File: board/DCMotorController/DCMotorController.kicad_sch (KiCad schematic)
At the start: 129 parts, among them J2 Conn_01x03_Female, M1+1 Conn_01x01_Female, M1-1 Conn_01x01_Female, M1_S1 Conn_01x03_Female, M1_S2 Conn_01x03_Female, M2+1 Conn_01x01_Female, M2-1 Conn_01x01_Female, M2_S1 Conn_01x03_Female, M2_S2 Conn_01x03_Female, Q1 Q_NMOS_GDS, Q10 Q_NMOS_GDS, Q11 Q_NMOS_GDS, Q12 Q_NMOS_GDS, Q13 Q_NMOS_GDS, Q14 Q_NMOS_GDS, Q15 Q_NMOS_GDS, Q16 Q_NMOS_GDS, Q2 Q_NMOS_GDS, Q3 Q_NMOS_GDS, Q4 Q_NMOS_GDS, Q5 Q_NMOS_GDS, Q6 Q_NMOS_GDS, Q7 Q_NMOS_GDS, Q8 Q_NMOS_GDS, Q9 Q_NMOS_GDS, U1 DS18B20, U10 TPS54360DDA, U2 IR2103, U3 IR2103, U4 ESP32-WROOM-32D, U5 IR2103, U6 IR2103, U7 TPS54360DDA, U8 AMS1117-3.3, U9 DS18B20

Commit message: first version + test firmeware
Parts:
- added C42, C43, C44: 1500uF, Capacitor_THT:C_Radial_D10.0mm_H12.5mm_P5.00mm, symbol Device:C_Polarized
- added D20: WS2812B, LED_SMD:LED_WS2812B_PLCC4_5.0x5.0mm_P3.2mm, symbol LED:WS2812B
- added R23, R24, R25, R26: 10k, Resistor_SMD:R_0603_1608Metric, symbol Device:R
- Boot1: LCSC storage -> C72443; LCSC_PART_NUMBER C72443 -> (none)
- C1, C2, C5: LCSC yes -> C49678; LCSC_PART_NUMBER C49678 -> (none)
- C10, C12, C15, C25, C28, C33: LCSC yes -> C14663; LCSC_PART_NUMBER C14663 -> (none)
- C11, C13, C14, C26, C27, C7, C8, C9: LCSC yes -> C13585; LCSC_PART_NUMBER C13585 -> (none)
- C16, C18, C37, C38: footprint Resistor_SMD:R_1206_3216Metric -> Capacitor_SMD:C_1206_3216Metric; LCSC fix footrpint -> C96123; LCSC_PART_NUMBER C96123 -> (none)
- C17: LCSC fix footprint -> C59461
- C19, C20, C31, C32: footprint Capacitor_SMD:C_0603_1608Metric -> Capacitor_SMD:C_1206_3216Metric; LCSC lcsc -> C920964; LCSC_PART_NUMBER C920964 -> (none)
- C21, C22, C35, C36: LCSC lcsc -> C1666
- C23: footprint Capacitor_THT:C_Radial_D18.0mm_H35.5mm_P7.50mm -> Capacitor_THT:CP_Radial_D25.0mm_P10.00mm_SnapIn; LCSC lcsc -> C316460
- C24, C34: LCSC yes -> C1631; LCSC_PART_NUMBER C1631 -> (none)
- C29, C39, C40, C41: LCSC yes -> C16780; LCSC_PART_NUMBER C16780 -> (none)
- C3, C4, C6: LCSC yes -> C5674; LCSC_PART_NUMBER C45783 -> (none)
- C30: LCSC lcsc -> C503217; LCSC_PART_NUMBER C503217 -> (none)
- D1, D11, D4, D8: LCSC yes -> C412437; LCSC_PART_NUMBER C412437 -> (none)
- D10, D12, D13, D2, D5, D6, D7, D9: LCSC yes -> C81598; LCSC_PART_NUMBER C81598 -> (none)
- D14, D15, D16, D17, D3: LCSC no -> C397601
- D18: LCSC no -> C85100; LCSC_PART_NUMBER C266541 -> (none)
- D19: LCSC yes -> C191023; LCSC_PART_NUMBER C191023 -> (none)
- L1: LCSC no -> C2761921
- L2: LCSC no -> C2847544
- Q1, Q10, Q11, Q12, Q13, Q14, Q15, Q16, Q2, Q3, Q4, Q5, Q6, Q7, Q8, Q9: LCSC (none) -> C110912; LCSC_PART_NUMBER C2838123 -> (none)
- R1, R17, R2: footprint Resistor_SMD:R_0805_2012Metric -> Resistor_SMD:R_0603_1608Metric; LCSC (none) -> C21190; LCSC_PART_NUMBER C95781 -> (none)
- R10, R3, R4, R5, R6, R7, R8, R9: value ~100ohm -> 15; LCSC (none) -> C22810
- R11: value 0ohm -> 15; footprint Resistor_SMD:R_0603_1608Metric_Pad0.98x0.95mm_HandSolder -> Resistor_SMD:R_0603_1608Metric; LCSC (none) -> C22810
- R12, R22: footprint Capacitor_SMD:C_0603_1608Metric -> Resistor_SMD:R_0603_1608Metric; LCSC (none) -> C22797
- R13: LCSC (none) -> C21190; LCSC_PART_NUMBER C95781 -> (none)
- R14, R15: LCSC (none) -> C21190; LCSC_PART_NUMBER C212284 -> (none)
- R16: LCSC (none) -> C25804; LCSC_PART_NUMBER C212284 -> (none)
- R18, R19, R20, R21: LCSC (none) -> C23254; LCSC_PART_NUMBER C23254 -> (none)
- Reset1: LCSC (none) -> C72443; LCSC_PART_NUMBER C72443 -> (none)
- Rvoltage1, Rvoltage2, Rvoltage4: footprint Capacitor_SMD:C_0603_1608Metric -> Resistor_SMD:R_0603_1608Metric
- Rvoltage3: footprint Capacitor_SMD:C_0603_1608Metric -> Resistor_SMD:R_0603_1608Metric; LCSC (none) -> C22797; LCSC_PART_NUMBER C22797 -> (none)
- U10, U7: LCSC yes -> C44377; LCSC_PART_NUMBER C44377 -> (none)
- U2, U3, U5, U6: LCSC (none) -> C111908; LCSC_PART_NUMBER C111908 -> (none)
- U4: LCSC (none) -> C529578; LCSC_PART_NUMBER C529578 -> (none)
- U8: LCSC yes -> C96123; LCSC_PART_NUMBER C6186 -> (none)
- renumbered J2 to GND_TX_RX1
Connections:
- net CUSTOM_GPIO12 is gone; now on net M1_S2: U4.14 (IO12)
- net PLANT_CTRL_PUMP_1 is gone; now on net M2_S2: U4.29 (IO5)
- net PUMP_ENABLE is gone; now on net M2_S1: U4.16 (IO13)
- net SENSORS_ENABLE is gone; now on net M1_S1: U4.13 (IO14)
- net 3_3V: now also D20.1 (VDD)
- net 5V: no longer U8.3 (VI)
- net GND: now also Boot1.1, C1.1, C42.2, C43.2, C44.2, D20.3 (VSS)
- net M1_S1: now also R23.2; no longer M1_S1.3 (Pin_3)
- net M1_S2: now also R24.2; no longer M1_S2.3 (Pin_3)
- net M2_S1: now also R25.2; no longer M2_S1.3 (Pin_3)
- net M2_S2: now also R26.2; no longer M2_S2.3 (Pin_3)
- net VIN: now also C42.1, C43.1, C44.1
- net VMosfet: now also U8.3 (VI)
- net PLANT0_MOIST: no longer names the net of U4.8 (IO32)
- net PLANT0_MOIST: now also D20.4 (DIN)
- new net: M1_S1.3 (Pin_3), R23.1
- new net: M1_S2.3 (Pin_3), R24.1
- new net: M2_S1.3 (Pin_3), R25.1
- new net: M2_S2.3 (Pin_3), R26.1
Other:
- moved on the sheet: M1_S1, M1_S2, M2_S1, M2_S2

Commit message: Allegro current sensor edition
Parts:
- removed C15: 100nF, Capacitor_SMD:C_0603_1608Metric, symbol Device:C
- removed C16, C18: 47uF, Capacitor_SMD:C_1206_3216Metric, symbol Device:C
- removed C19, C20: 2.2uF 60V, Capacitor_SMD:C_1206_3216Metric, symbol Device:C
- removed C21, C22: 39pf, Capacitor_SMD:C_0603_1608Metric, symbol Device:C
- removed C24: 6800pF, Capacitor_SMD:C_0603_1608Metric, symbol Device:C
- removed C30: 1000uF, Capacitor_THT:CP_Radial_D10.0mm_P5.00mm, symbol Device:CP
- removed C44: 1500uF, Capacitor_THT:C_Radial_D10.0mm_H12.5mm_P5.00mm, symbol Device:C_Polarized
- removed D18: B560C, Diode_SMD:D_SMC_Handsoldering, symbol Device:D
- removed L1: 8.2uH, Inductor_SMD:L_12x12mm_H8mm, symbol Device:L
- removed R12: 13k, Resistor_SMD:R_0603_1608Metric, symbol Device:R
- removed R19, R21: 82k, Resistor_SMD:R_0603_1608Metric_Pad0.98x0.95mm_HandSolder, symbol Device:R
- removed Rvoltage1: 5.24*Rvoltage2 (5,6 - 7.5), Resistor_SMD:R_0603_1608Metric, symbol Device:R
- removed Rvoltage2: 1k 1.4k, Resistor_SMD:R_0603_1608Metric, symbol Device:R
- removed U7: TPS54360DDA, Package_SO:TI_SO-PowerPAD-8_ThermalVias, symbol Regulator_Switching:TPS54360DDA
- added C? (x2): 100nF, Capacitor_SMD:C_0603_1608Metric, symbol Device:C
- added R? (x2): 1k, Resistor_SMD:R_0603_1608Metric, symbol Device:R
- added U11, U7: ACS758xCB-100B-PFF, Sensor_Current:Allegro_CB_PFF, symbol Sensor_Current:ACS758xCB-100B-PFF
- C23: footprint Capacitor_THT:CP_Radial_D25.0mm_P10.00mm_SnapIn -> Capacitor_THT:CP_Radial_D12.5mm_P5.00mm
- C42, C43: footprint Capacitor_THT:C_Radial_D10.0mm_H12.5mm_P5.00mm -> Capacitor_THT:CP_Radial_D12.5mm_P5.00mm
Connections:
- net 3_3V: now also U11.1 (VCC), U7.1 (VCC)
- net GND: now also C?.1, C?.1, U11.2 (GND), U7.2 (GND)
- net at C11.2, Q11.3 (S), Q12.3 (S)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: now also U11.5 (IP-); no longer M1-1.1 (Pin_1)
- net at C27.2, Q10.3 (S), Q13.2 (D)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: now also U7.4 (IP+); no longer M2-1.1 (Pin_1)
- net CUSTOM_GPIO2: no longer names the net of U4.24 (IO2)
- net CUSTOM_GPIO34 renamed M1_Sense
- net M1_Sense: now also C?.2, R?.2
- net CUSTOM_GPIO35 renamed M2_Sense
- net M2_Sense: now also C?.2, R?.2
- net PLANT1_MOIST: no longer names the net of U4.9 (IO33)
- net PLANT5_MOIST: no longer names the net of U4.5 (SENSOR_VN)
- net PLANT6_MOIST: no longer names the net of U4.4 (SENSOR_VP)
- new net: R?.1, U7.3 (VIOUT)
- new net: M2-1.1 (Pin_1), U7.5 (IP-)
- new net: R?.1, U11.3 (VIOUT)
- new net: M1-1.1 (Pin_1), U11.4 (IP+)
- no-connect marks 6 -> 10
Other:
- note removed: "5V 3.5A downstepper"
- moved on the sheet: C31, C32, C33, C34, C35, C36, C37, C38, D19, L2, M1+1, M1-1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

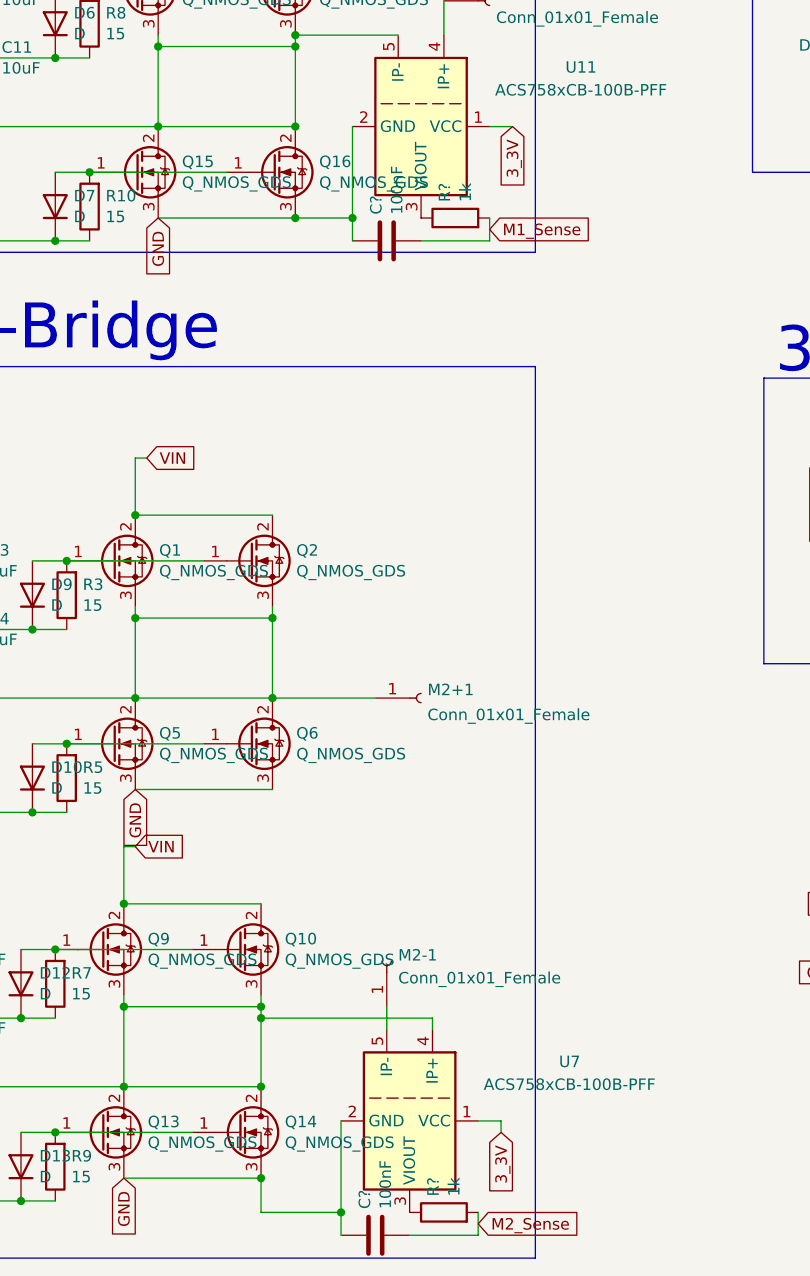
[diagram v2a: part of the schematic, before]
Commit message: added voltage converter
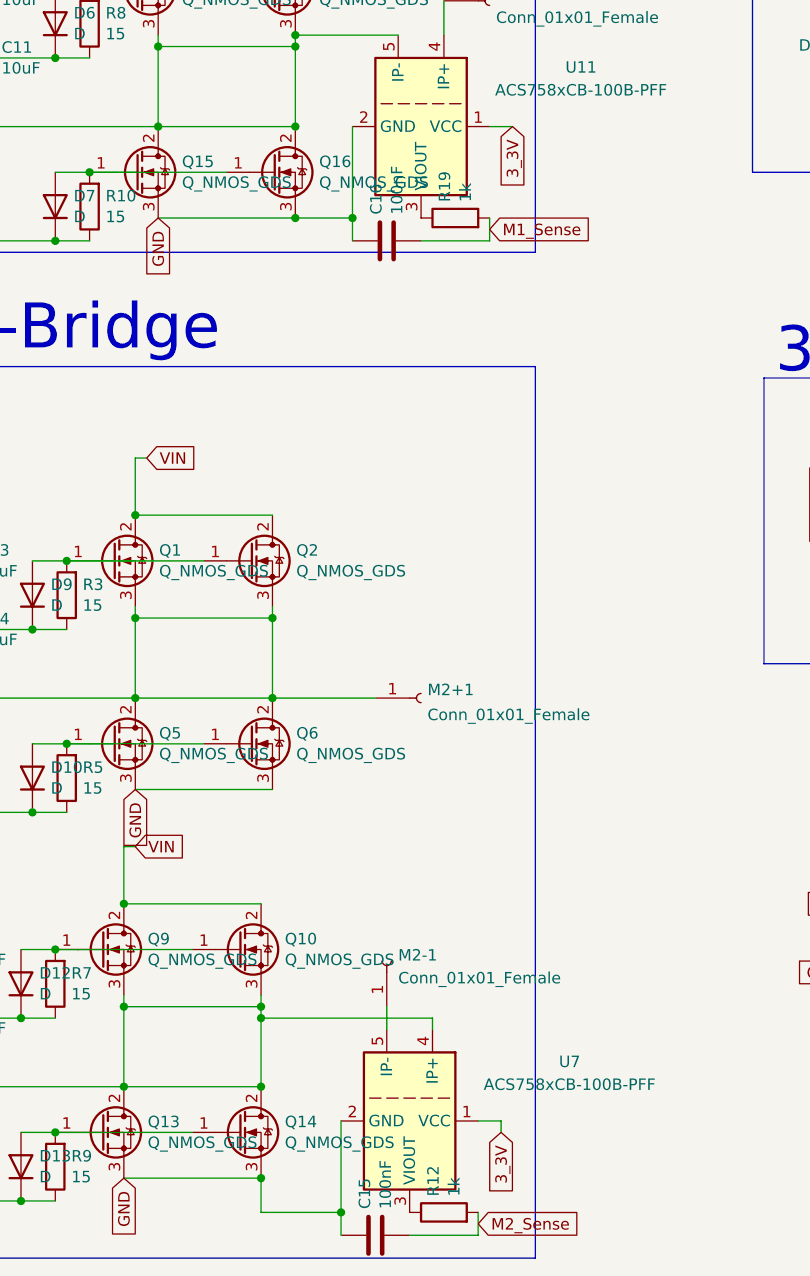
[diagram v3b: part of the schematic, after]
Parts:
- gave numbers to parts that had none: 4
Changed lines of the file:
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@@
   (symbol (lib_id "Device:R") (at 339.09 125.73 90) (unit 1)
     (in_bom yes) (on_board yes)
-    (property "Reference" "R?" (id 0) (at 337.9216 123.952 0)
+    (property "Reference" "R19" (id 0) (at 337.9216 123.952 0)
       (effects (font (size 1.27 1.27)) (justify left))
     )
@@
   (symbol (lib_id "Device:C") (at 330.2 238.76 90) (unit 1)
     (in_bom yes) (on_board yes)
-    (property "Reference" "C?" (id 0) (at 329.0316 235.839 0)
+    (property "Reference" "C15" (id 0) (at 329.0316 235.839 0)
       (effects (font (size 1.27 1.27)) (justify left))
     )
@@
   (symbol (lib_id "Device:R") (at 337.82 236.22 90) (unit 1)
     (in_bom yes) (on_board yes)
-    (property "Reference" "R?" (id 0) (at 336.6516 234.442 0)
+    (property "Reference" "R12" (id 0) (at 336.6516 234.442 0)
       (effects (font (size 1.27 1.27)) (justify left))
     )
@@
   (symbol (lib_id "Device:C") (at 331.47 128.27 90) (unit 1)
     (in_bom yes) (on_board yes)
-    (property "Reference" "C?" (id 0) (at 330.3016 125.349 0)
+    (property "Reference" "C16" (id 0) (at 330.3016 125.349 0)
       (effects (font (size 1.27 1.27)) (justify left))
     )
@@
       (reference "C14") (unit 1) (value "10uF") (footprint "Capacitor_SMD:C_1206_3216Metric")
     )
+    (path "/2d32893f-12de-4032-bc8a-a3a09e8673ca"
+      (reference "C15") (unit 1) (value "100nF") (footprint "Capacitor_SMD:C_0603_1608Metric")
+    )
+    (path "/a648105e-3142-454a-80fd-a7386ac44203"
+      (reference "C16") (unit 1) (value "100nF") (footprint "Capacitor_SMD:C_0603_1608Metric")
+    )
     (path "/00000000-0000-0000-0000-000061ce86a1"
       (reference "C17") (unit 1) (value "22uF") (footprint "Capacitor_SMD:C_0603_1608Metric")
@@
       (reference "C43") (unit 1) (value "1500uF") (footprint "Capacitor_THT:CP_Radial_D12.5mm_P5.00mm")
     )
-    (path "/2d32893f-12de-4032-bc8a-a3a09e8673ca"
-      (reference "C?") (unit 1) (value "100nF") (footprint "Capacitor_SMD:C_0603_1608Metric")
-    )
-    (path "/a648105e-3142-454a-80fd-a7386ac44203"
-      (reference "C?") (unit 1) (value "100nF") (footprint "Capacitor_SMD:C_0603_1608Metric")
-    )
     (path "/3ff7dd96-621c-4a88-987a-6befb4074700"
       (reference "D1") (unit 1) (value "US1A") (footprint "Diode_SMD:D_SMA")
@@
       (reference "R11") (unit 1) (value "15") (footprint "Resistor_SMD:R_0603_1608Metric")
     )
+    (path "/8bdfec95-3190-4dff-9c58-776b290ebfa4"
+      (reference "R12") (unit 1) (value "1k") (footprint "Resistor_SMD:R_0603_1608Metric")
+    )
     (path "/00000000-0000-0000-0000-000060983db3"
       (reference "R13") (unit 1) (value "1k") (footprint "Resistor_SMD:R_0603_1608Metric")
@@
       (reference "R18") (unit 1) (value "82k") (footprint "Resistor_SMD:R_0603_1608Metric_Pad0.98x0.95mm_HandSolder")
     )
+    (path "/0a83d85f-0555-46a5-9d87-de66786a4954"
+      (reference "R19") (unit 1) (value "1k") (footprint "Resistor_SMD:R_0603_1608Metric")
+    )
     (path "/e56fb342-8e86-43b1-a6c4-bec8e7244baa"
       (reference "R20") (unit 1) (value "82k") (footprint "Resistor_SMD:R_0603_1608Metric_Pad0.98x0.95mm_HandSolder")
@@
       (reference "R26") (unit 1) (value "10k") (footprint "Resistor_SMD:R_0603_1608Metric")
     )
-    (path "/0a83d85f-0555-46a5-9d87-de66786a4954"
-      (reference "R?") (unit 1) (value "1k") (footprint "Resistor_SMD:R_0603_1608Metric")
-    )
-    (path "/8bdfec95-3190-4dff-9c58-776b290ebfa4"
-      (reference "R?") (unit 1) (value "1k") (footprint "Resistor_SMD:R_0603_1608Metric")
-    )
     (path "/00000000-0000-0000-0000-0000603df238"

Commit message: updated with newer 5 and 3 v supply, potentiometer supply optional added, current sensor rearangement
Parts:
- removed 1WIRE1: Conn_01x03, Connector_JST:JST_EH_B3B-EH-A_1x03_P2.50mm_Vertical, symbol Connector_Generic:Conn_01x03
- removed C29, C39, C40, C41: 47uF, Capacitor_SMD:C_0805_2012Metric, symbol Device:C
- removed D3: BAS40-04, Package_TO_SOT_SMD:SOT-23, symbol Diode:BAS40-04
- removed U1: DS18B20, Package_TO_SOT_THT:TO-92_Inline, symbol Sensor_Temperature:DS18B20
- removed U8: AMS1117-3.3, Package_TO_SOT_SMD:SOT-223-3_TabPin2, symbol Regulator_Linear:AMS1117-3.3
- added 3_3_En1, 3_3_En2, 3_3_En3, 3_3_En4: (no value), Jumper:SolderJumper-2_P1.3mm_Open_RoundedPad1.0x1.5mm, symbol Jumper:SolderJumper_2_Open
- added C18: 22uF, Capacitor_SMD:C_0603_1608Metric, symbol Device:C
- added R21: 10k, Resistor_SMD:R_0603_1608Metric, symbol Device:R
- added R27: 2k7, Resistor_SMD:R_0603_1608Metric, symbol Device:R
- added U12: SPX3819M5-L-5-0, Package_TO_SOT_SMD:SOT-23-5, symbol Regulator_Linear:SPX3819M5-L-5-0
- added U8: SPX3819M5-L-3-3, Package_TO_SOT_SMD:SOT-23-5, symbol Regulator_Linear:SPX3819M5-L-3-3
- BZ1: footprint Buzzer_Beeper:Buzzer_TDK_PS1240P02BT_D12.2mm_H6.5mm -> Buzzer_Beeper:Buzzer_15x7.5RM7.6
- R19, R2: value 1k -> 2k7
- R26: value 10k -> 2k7; LCSC C25804 -> C21190
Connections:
- net 3_3V: now also 3_3_En1.1 (A), 3_3_En2.1 (A), 3_3_En3.1 (A), 3_3_En4.1 (A), U8.5 (OUT); no longer R1.2, U11.1 (VCC), U7.1 (VCC)
- net 5V: now also U11.1 (VCC), U7.1 (VCC), C18.1, U12.5 (OUT); no longer D14.2, D15.2, D16.2, D17.2, M1_S1.2 (Pin_2), M1_S2.2 (Pin_2), M2_S1.2 (Pin_2), M2_S2.2 (Pin_2)
- net GND: now also C15.2, C16.2, R19.1, R2.1, C18.2, U12.2 (GND), U8.2 (GND); no longer C15.1, C16.1
- net M1_S2: now also R21.2; no longer R24.2
- net M1_Sense: now also C16.1, R1.2; no longer C16.2, R19.2
- net M2_S1: now also R24.2; no longer R25.2
- net M2_S2: now also R25.2; no longer R26.2
- net M2_Sense: now also C15.1; no longer C15.2
- net Temp: no longer R2.2
- net VMosfet: now also U12.1 (IN), U12.3 (EN), U8.1 (IN), U8.3 (EN)
- net at R1.1: now also R19.2, R27.1; no longer R2.1
- net at M1_S2.3 (Pin_3): now also R21.1; no longer R24.1
- net at M2_S1.3 (Pin_3): now also R24.1; no longer R25.1
- net at M2_S2.3 (Pin_3): now also R25.1; no longer R26.1
- net at U7.3 (VIOUT): now also R26.2; no longer R12.1
- net at U11.3 (VIOUT): now also R27.2; no longer R19.1
- net SCL: no longer names the net of U4.27 (IO16)
- net SDA: no longer names the net of U4.28 (IO17)
- new net: 3_3_En1.2 (B), D14.2, M1_S1.2 (Pin_2)
- new net: 3_3_En2.2 (B), D15.2, M1_S2.2 (Pin_2)
- new net: 3_3_En3.2 (B), D16.2, M2_S1.2 (Pin_2)
- new net: 3_3_En4.2 (B), D17.2, M2_S2.2 (Pin_2)
- new net: R12.1, R2.2, R26.1
- no-connect marks 10 -> 16
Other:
- note added: "5v LDO"
- moved on the sheet: C13, C14, C15, C25, C26, C27, C28, D10, D11, D12, D13, D14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

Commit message: update to newer current sensoring
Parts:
- removed C42: 1500uF, Capacitor_THT:CP_Radial_D12.5mm_P5.00mm, symbol Device:C_Polarized
- removed GND1, VIN1: Conn_01x01_Female, Wire-Solder:60A_Wire_solder, symbol Connector:Conn_01x01_Female
- removed R1: 1k, Resistor_SMD:R_0603_1608Metric, symbol Device:R
- removed R2, R26, R27: 2k7, Resistor_SMD:R_0603_1608Metric, symbol Device:R
- removed U11, U7: ACS758xCB-100B-PFF, Sensor_Current:Allegro_CB_PFF, symbol Sensor_Current:ACS758xCB-100B-PFF
- removed U12: SPX3819M5-L-5-0, Package_TO_SOT_SMD:SOT-23-5, symbol Regulator_Linear:SPX3819M5-L-5-0
- added C19: 100nF, Capacitor_SMD:C_0603_1608Metric, symbol Device:C
- added D3: US1A, Diode_SMD:D_SMA, symbol Diode:US1A
- added Di_+_-1: Conn_01x03_Female, Connector_PinHeader_2.54mm:PinHeader_1x03_P2.54mm_Vertical, symbol Connector:Conn_01x03_Male
- added J1: Conn_01x02, Connector_AMASS:AMASS_XT60-M_1x02_P7.20mm_Vertical, symbol Connector_Generic:Conn_01x02
- added R1, R2: R_Shunt, Wire-Solder:Shunt 1moh 5W, symbol Device:R_US
- added U1, U7: INA180A1, Package_TO_SOT_SMD:SOT-23-5, symbol Amplifier_Current:INA180A1
- BZ1: footprint Buzzer_Beeper:Buzzer_15x7.5RM7.6 -> Wire-Solder:Buzzer_12x7.5
- C1, C2, C5: footprint Capacitor_SMD:C_0805_2012Metric -> Capacitor_SMD:C_0603_1608Metric; LCSC C49678 -> C14663
- C18: value 22uF -> 100nF; LCSC C59461 -> C14663
- C23, C43: value 1500uF -> 750uF
- R12: value 1k -> 10k; LCSC C21190 -> C25804
- R19: value 2k7 -> 10k; LCSC C21190 -> C25804
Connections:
- net 5V is gone; now on net GND: C18.1
- net 3_3V: now also C15.1, C16.1, Di_+_-1.2 (Pin_2), U1.5 (V+), U7.5 (V+)
- net GND: now also C19.1, Di_+_-1.1 (Pin_1), J1.1 (Pin_1), R1.2, R2.2, U1.2 (GND), U1.4 (-), U7.2 (GND), U7.4 (-); no longer C18.2, C23.2, C43.2, Q13.3 (S), Q14.3 (S), Q15.3 (S), Q16.3 (S), Q5.3 (S), Q6.3 (S), Q7.3 (S), Q8.3 (S), R19.1
- net M1_Sense: now also C18.2, R12.1; no longer C16.1
- net M2_Sense: now also R19.1, C19.2; no longer C15.1, R12.2
- net VIN: now also D3.2 (A), J1.2 (Pin_2); no longer C31.1, C32.1, U10.2 (VIN)
- net at C11.2, Q11.3 (S), Q12.3 (S)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: now also M1-1.1 (Pin_1)
- net at C27.2, Q10.3 (S), Q13.2 (D)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: now also M2-1.1 (Pin_1)
- net at R19.2: now also U7.1
- net at D20.2 (DOUT): now also Di_+_-1.3 (Pin_3)
- new net: C31.1, C32.1, D3.1 (K), U10.2 (VIN)
- new net: R12.2, U1.1
- new net M1_Shunt: C23.2, Q15.3 (S), Q16.3 (S), Q7.3 (S), Q8.3 (S), R1.1, U1.3 (+)
- new net M2_Shunt: C43.2, Q13.3 (S), Q14.3 (S), Q5.3 (S), Q6.3 (S), R2.1, U7.3 (+)
- no-connect marks 16 -> 14
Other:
- note added: "Current Sensors"
- note removed: "5v LDO"
- moved on the sheet: C23, C43, M1-1, M2-1
